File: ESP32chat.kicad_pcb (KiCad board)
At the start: 4 copper layers, 121.9 x 101.6 mm, 178 parts, among them J1 CONN_021X02_NO_SILK, J2 CONN_01, J3 CONN_01, J4 CONN_021X02_NO_SILK, J5 CONN_021X02_NO_SILK, J6 CONN_021X02_NO_SILK, Q1 Q_PMOS_DGS, Q2 BSS123, Q3 Si1308, SW1 SW_DIP_x01, U1 MCP73831T-2ACI/OT, U10 MOUNTINGHOLE2.0, U11 MOUNTINGHOLE2.0, U12 MOUNTINGHOLE2.0, U13 MOUNTINGHOLE2.0, U14 MOUNTINGHOLE2.0, U15 MOUNTINGHOLE2.0, U16 MOUNTINGHOLE2.0, U17 MOUNTINGHOLE2.0, U18 BGU8019, U19 LM75B, U2 TP4056, U20 ATGM336H-5N31, U21 QMC5883L, U22 FPCConn, U3 ESP32, U4 FS8205A, U5 DW01, U6 RT9013, U7 RFM69HCW, U8 tp4056_KoreanHropartsElecTYPE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, U9 BUZZER, X1 uFL

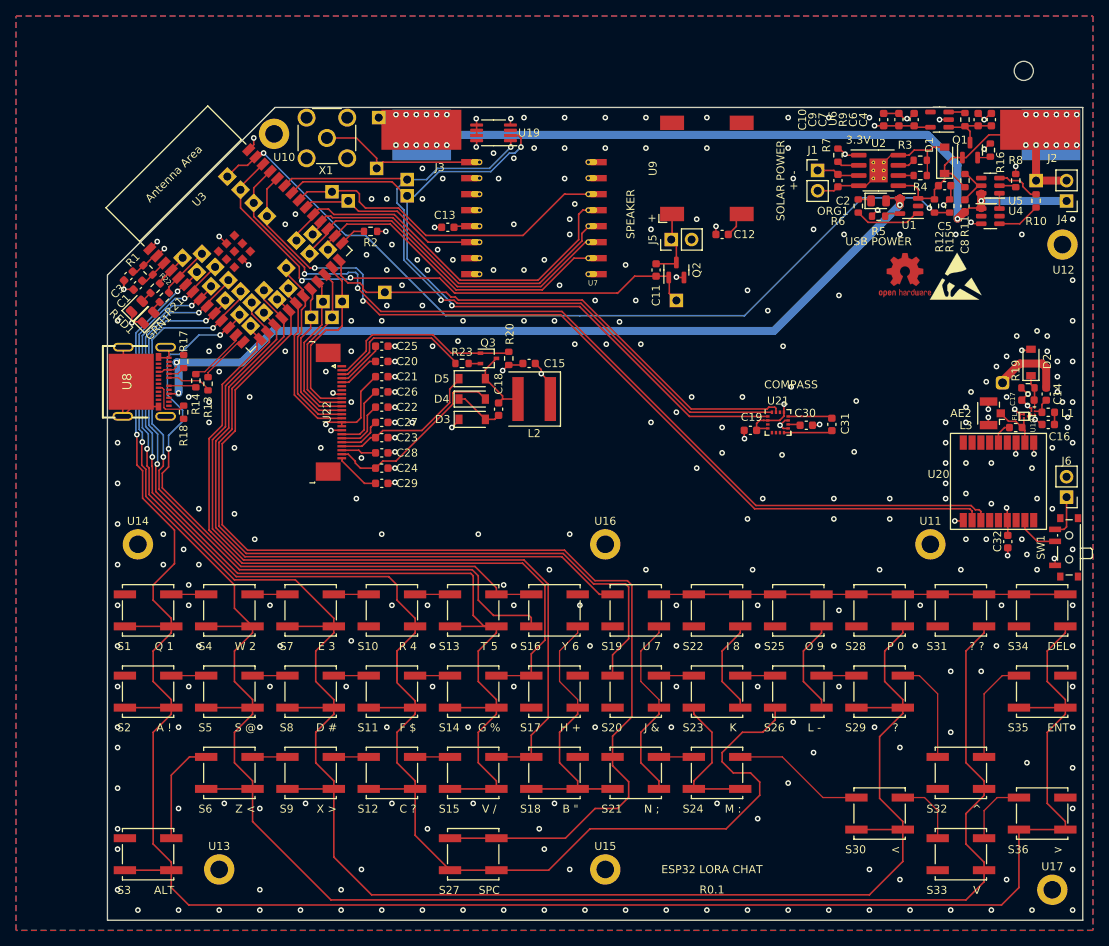
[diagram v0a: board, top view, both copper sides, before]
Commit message: Some corrections to align with JLCPCB verification, added I2C memory chip.
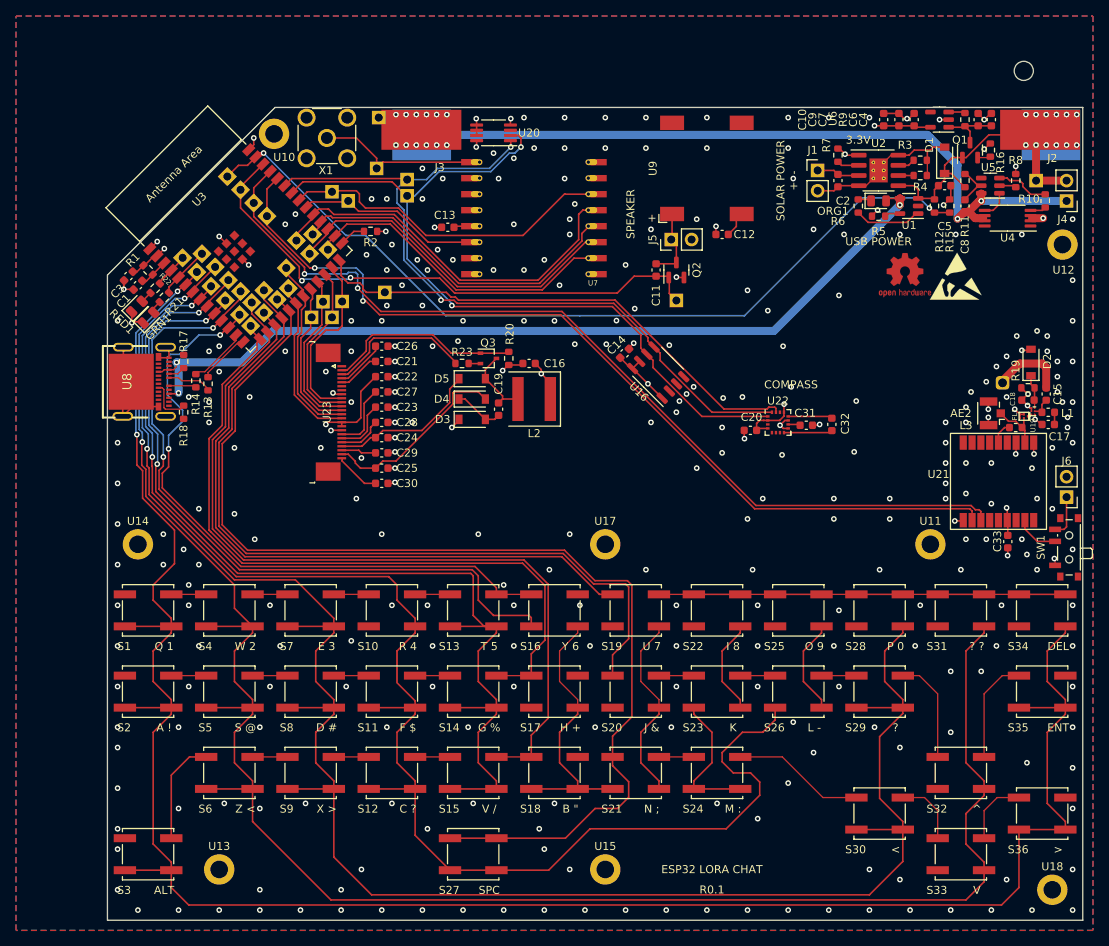
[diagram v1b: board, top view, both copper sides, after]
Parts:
- added C14: 100n, Capacitor_SMD:C_0603_1608Metric, F.Cu at (126.9, 87.9)
- added U16: MB85RC64, Package_SO:SOP-8_3.9x4.9mm_P1.27mm, F.Cu at (131.1, 90.3)
- U4: footprint Package_TO_SOT_SMD:SOT-23-6 -> Package_SO:TSSOP-8_4.4x3mm_P0.65mm
- moved U4 2.17 mm to (174.8, 71.0), turned to 180 degrees
- moved R10 1.14 mm to (179.5, 68.8)
- renumbered C14 to C15, C15 to C16, C16 to C17, C17 to C18, C18 to C19, C19 to C20, C20 to C21, C21 to C22, C22 to C23, C23 to C24, C24 to C25, C25 to C26, C26 to C27, C27 to C28, C28 to C29, C29 to C30, C30 to C31, C31 to C32, C32 to C33, U16 to U17, U17 to U18, U18 to U19, U19 to U20, U20 to U21, U21 to U22, U22 to U23
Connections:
- U4 pad 1: /BAT- -> unconnected-(U4-Pad1)
- U4 pad 2: unconnected-(U4-Pad2) -> GND
- U4 pad 5: unconnected-(U4-Pad5) -> /G1
- U4 pad 6: /G1 -> /BAT-
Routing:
- net +3.3V: track 46.7 -> 55.3 mm, vias 11 -> 12
- net /G2: track 5.42 -> 1.99 mm
- net GND: track 93.5 -> 95.6 mm, vias 316 -> 319
- net /G1: track 1.91 -> 3.51 mm
- net /I2S_SCL: track 96.3 -> 97.8 mm
- net /OC: track 5.63 -> 6.77 mm
- net /I2S_SDA: track 96.3 -> 97.1 mm
- net /BAT-: track 101.2 -> 101.9 mm

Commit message: Updated kepad layout
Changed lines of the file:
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@@
     (at 138.43 130.175)
     (tags "tactile switch")
-    (property "Field5" "K ")
+    (property "Field5" "K *")
     (property "LCSC" "C318886")
     (property "Sheetfile" "ESP32chat.kicad_sch")
@@
     (at 168.91 120.015)
     (tags "tactile switch")
-    (property "Field5" "? ?")
+    (property "Field5" "' \"")
     (property "LCSC" "C318886")
     (property "Sheetfile" "ESP32chat.kicad_sch")
@@
     (at 158.75 130.175)
     (tags "tactile switch")
-    (property "Field5" "?")
+    (property "Field5" ". +")
     (property "LCSC" "C318886")
     (property "Sheetfile" "ESP32chat.kicad_sch")
@@
     (at 138.43 140.335)
     (tags "tactile switch")
-    (property "Field5" "M :")
+    (property "Field5" "M /")
     (property "LCSC" "C318886")
     (property "Sheetfile" "ESP32chat.kicad_sch")
@@
     (at 107.95 140.335)
     (tags "tactile switch")
-    (property "Field5" "V /")
+    (property "Field5" "V ~")
     (property "LCSC" "C318886")
     (property "Sheetfile" "ESP32chat.kicad_sch")
@@
     (at 128.27 140.335)
     (tags "tactile switch")
-    (property "Field5" "N ;")
+    (property "Field5" "N :")
     (property "LCSC" "C318886")
     (property "Sheetfile" "ESP32chat.kicad_sch")
@@
     (at 118.11 140.335)
     (tags "tactile switch")
-    (property "Field5" "B \"")
+    (property "Field5" "B ;")
     (property "LCSC" "C318886")
     (property "Sheetfile" "ESP32chat.kicad_sch")
@@
     (at 118.11 130.175)
     (tags "tactile switch")
-    (property "Field5" "H +")
+    (property "Field5" "H ^")
     (property "LCSC" "C318886")
     (property "Sheetfile" "ESP32chat.kicad_sch")
